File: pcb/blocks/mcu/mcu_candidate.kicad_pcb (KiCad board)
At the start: 6 copper layers, 164 x 234 mm, 10 parts, among them SW1 ?, SW2 ?, U1 ?

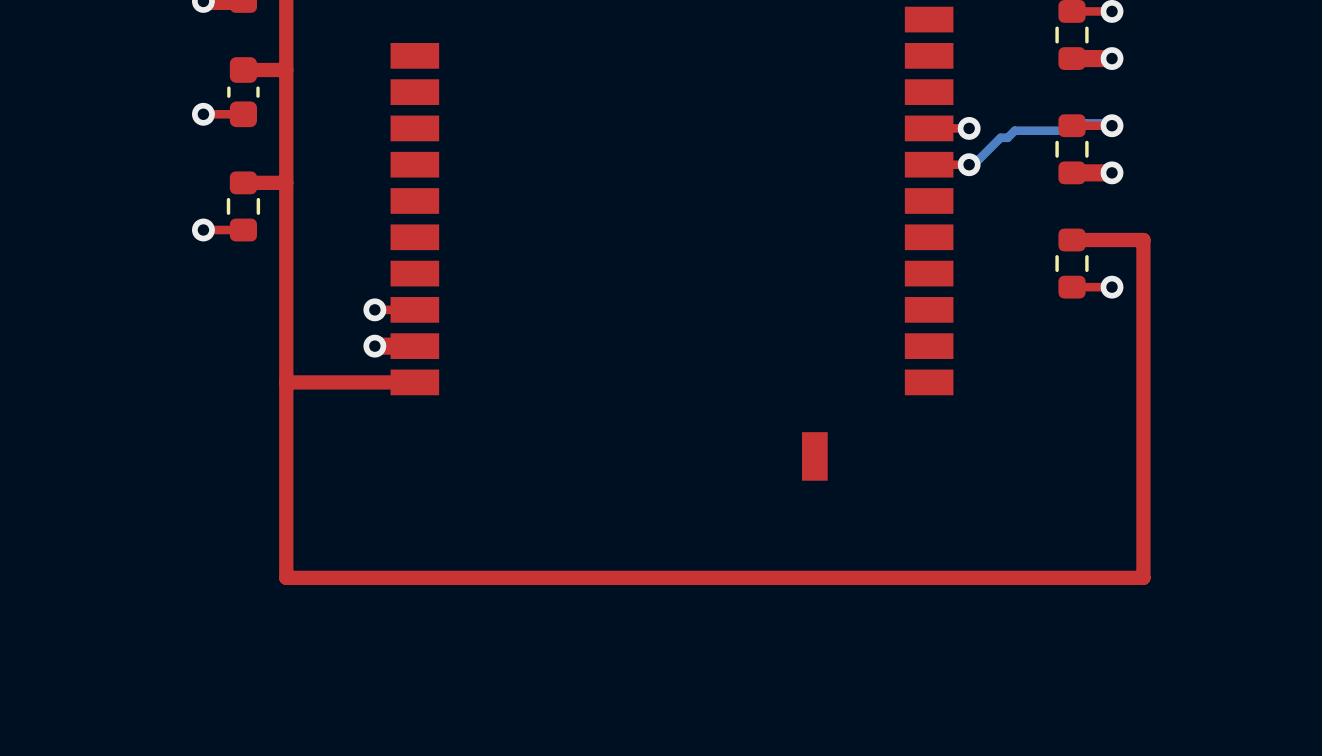
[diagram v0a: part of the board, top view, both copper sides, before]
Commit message: fix(mcu): schematic parity and real SW1/SW2 switch footprint
- block_source.build_strict_pin_map: one entry per unique (reference, pin),
  deduping repeated same-number pads and unconnected; a real switch exposes
  pads 1,1,2,2 and the per-physical-pad emission failed the design-bundle
  gate as duplicate_map. The Rust gate is unchanged and still rejects a
  genuine split pad.
- gen_pcb_skeleton.generate_candidate_board: optional values map sets the
  footprint Value from default.csv part identity (was '?').
- gen_schematics: flat strict-candidate layout with unscoped global labels,
  so net names are 'vcc' not '/MCU/vcc' and single-node compiled nets keep
  their pin; production hierarchy is unchanged.
- block_native._electrical_census: collapse repeated same-number pads to one
  electrical identity for the block judge, retaining pads_all for routing.
- apparatus run mcu-20260910-b: real-switch placement and every-physical-pad
  routing; native check 3x = DRC 0 / unconnected 0 / parity 0 / judge pass.
- package pcb/blocks/mcu re-admitted; ASSISTED-PACKAGE.json updated.

The elec/src/components.ato switch-footprint fix is a concurrent working-tree
change treated as fixed input and is intentionally not part of this commit.
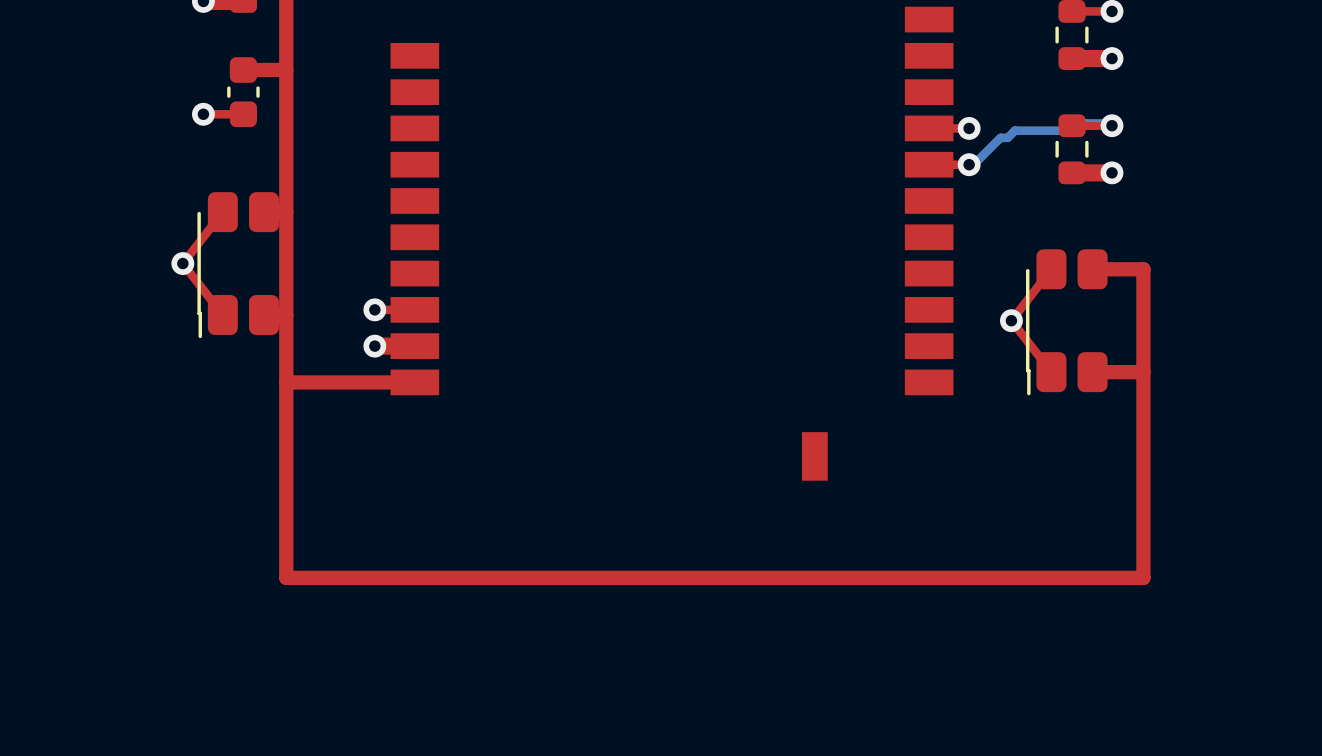
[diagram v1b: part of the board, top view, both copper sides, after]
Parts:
- C1: value ? -> C0603C104K5RACTU
- C2: value ? -> GRM21BR71A106KE51L
- C3: value ? -> GRM188R71A105KA61D
- R1, R2: value ? -> RC0603FR-0710KL
- R3, R4: value ? -> RC0603FR-074K7L
- SW1, SW2: value ? -> EVQ-P7A01P; footprint Resistor_SMD:R_0603_1608Metric -> Button_Switch_SMD:SW_SPST_EVQP7A
- U1: value ? -> ESP32-S3-WROOM-1-N8R8
- moved SW1 2.00 mm to (20.0, 56.0)
- moved SW2 2.00 mm to (49.0, 58.0)
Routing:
- net en: track 23.1 -> 27.9 mm
- net io0: track 24.0 -> 26.3 mm
